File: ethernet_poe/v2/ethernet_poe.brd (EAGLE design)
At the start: 45.5 x 50.5 mm, 86 parts, among them J3 ARJM11C7-104-AB-EW2, Q1 BSR16, U1 AZ1117EH-3.3TRG1, U2 IFX91041, U3 W5500, U4 TPS26600PWPR, X1 25MHz

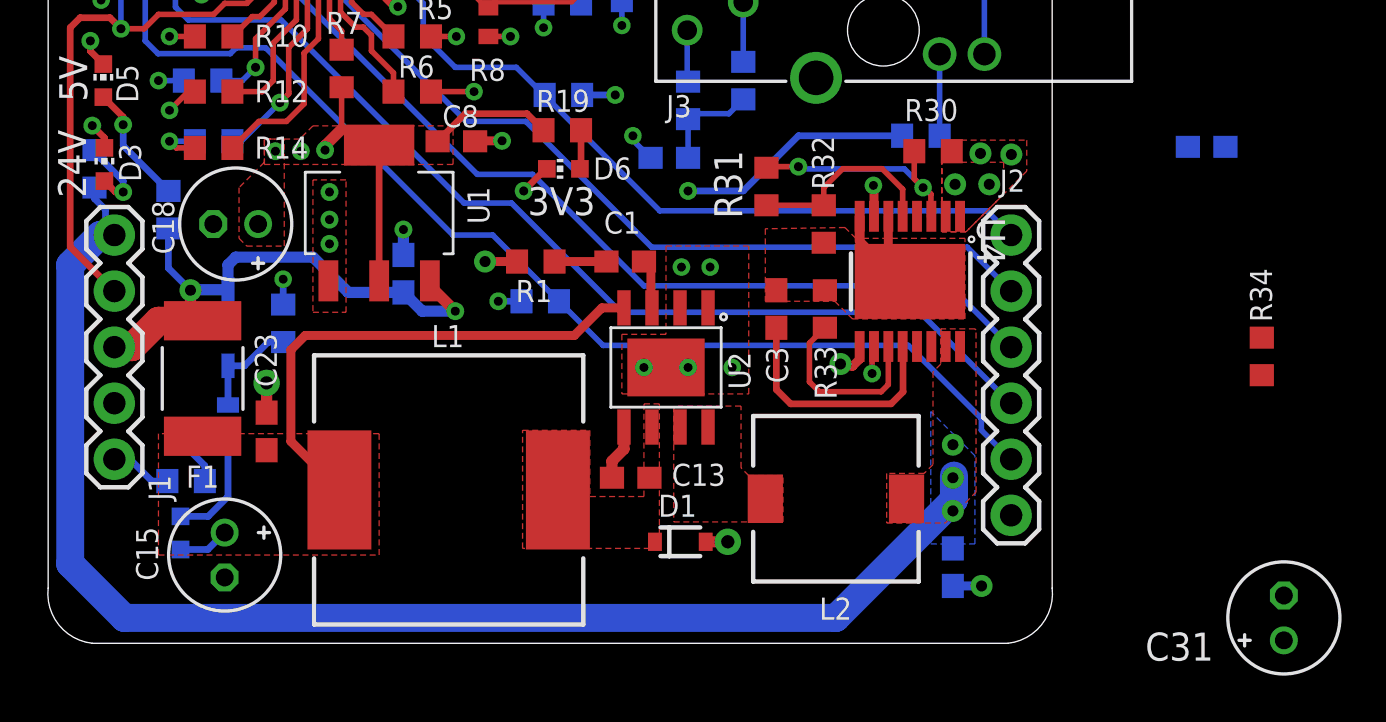
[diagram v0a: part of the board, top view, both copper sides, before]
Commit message: Placed + routed bulk 24v capacitor
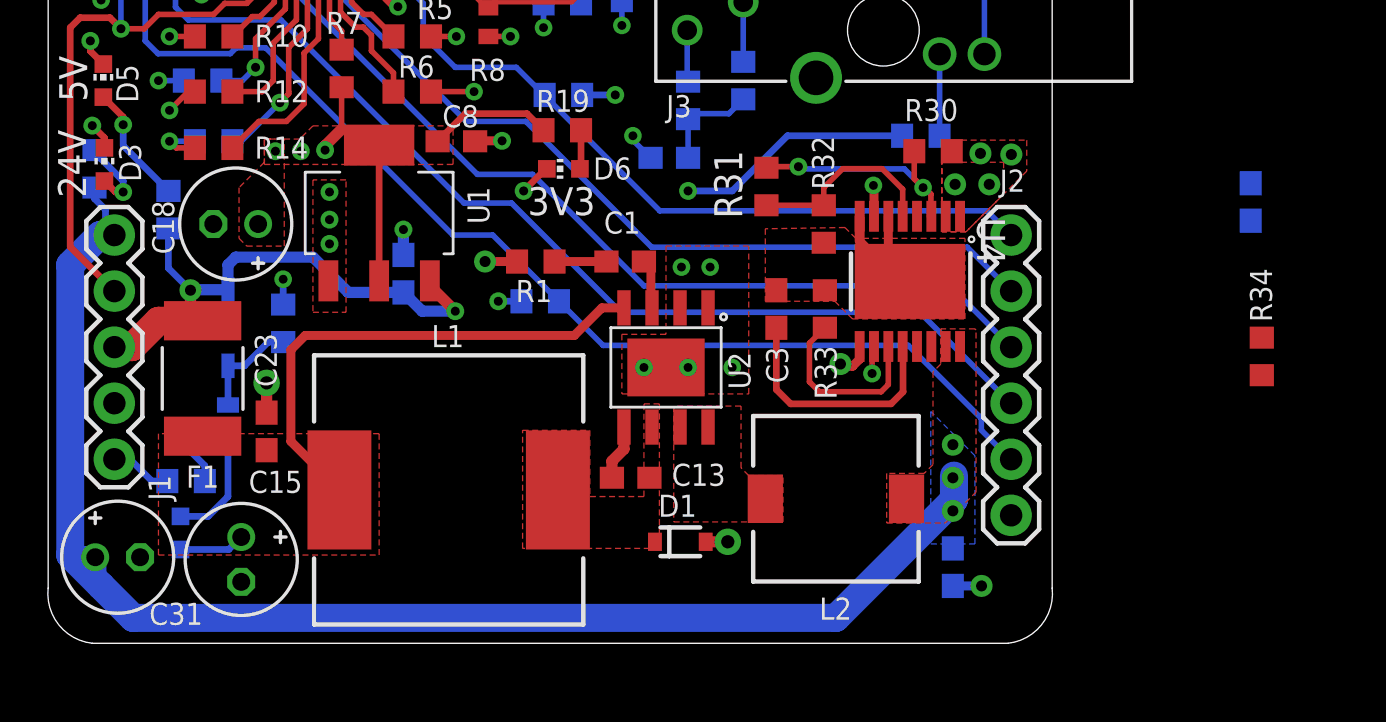
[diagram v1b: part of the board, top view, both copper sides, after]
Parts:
- moved C31 52.9 mm to (2.15, 3.40), turned to 0 degrees
- moved C30 3.20 mm to (53.5, 19.5), turned to 270 degrees
- moved C15 0.78 mm to (7.75, 3.30)
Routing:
- net +24V_FUSE: track 63.2 -> 65.6 mm
- net +5V_PREFUSE: track 25.5 -> 26.1 mm
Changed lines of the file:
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@@
 <attribute name="VALUE" x="13.195" y="15.615" size="1.27" layer="28" rot="MR90"/>
 </element>
-<element name="C15" library="rcl" library_urn="urn:adsk.eagle:library:334" package="E2-5" package3d_urn="urn:adsk.eagle:package:23346/2" value="100uF" x="7" y="3.5" smashed="yes" rot="R270">
-<attribute name="NAME" x="3.984" y="2.34" size="1" layer="25" font="vector" rot="R90"/>
-<attribute name="POPULARITY" value="7" x="7" y="3.5" size="1.778" layer="27" rot="R270" display="off"/>
-<attribute name="SPICEPREFIX" value="C" x="7" y="3.5" size="1.778" layer="27" rot="R270" display="off"/>
-<attribute name="VALUE" x="4.841" y="0.96" size="1.27" layer="27" ratio="10" rot="R270"/>
+<element name="C15" library="rcl" library_urn="urn:adsk.eagle:library:334" package="E2-5" package3d_urn="urn:adsk.eagle:package:23346/2" value="100uF" x="7.75" y="3.3" smashed="yes" rot="R270">
+<attribute name="NAME" x="8.09" y="6.316" size="1" layer="25" font="vector"/>
+<attribute name="POPULARITY" value="7" x="7.75" y="3.3" size="1.778" layer="27" rot="R270" display="off"/>
+<attribute name="SPICEPREFIX" value="C" x="7.75" y="3.3" size="1.778" layer="27" rot="R270" display="off"/>
+<attribute name="VALUE" x="5.591" y="0.76" size="1.27" layer="27" ratio="10" rot="R270"/>
 </element>
 <element name="J1" library="SparkFun-Connectors" package="1X05" package3d_urn="urn:adsk.eagle:package:38104/1" value="" x="2" y="18" smashed="yes" rot="R270">
@@
 <attribute name="VALUE" x="33.905" y="14.015" size="1.27" layer="27" rot="R90"/>
 </element>
-<element name="C30" library="rcl" library_urn="urn:adsk.eagle:library:334" package="C0603" package3d_urn="urn:adsk.eagle:package:23616/2" value="1uF" x="51.5" y="22" smashed="yes" rot="MR180">
-<attribute name="NAME" x="50.865" y="21.365" size="1.27" layer="26" rot="MR180"/>
-<attribute name="POPULARITY" value="37" x="51.5" y="22" size="1.778" layer="28" rot="MR180" display="off"/>
-<attribute name="SPICEPREFIX" value="C" x="51.5" y="22" size="1.778" layer="28" rot="MR180" display="off"/>
-<attribute name="VALUE" x="50.865" y="23.905" size="1.27" layer="28" rot="MR180"/>
+<element name="C30" library="rcl" library_urn="urn:adsk.eagle:library:334" package="C0603" package3d_urn="urn:adsk.eagle:package:23616/2" value="1uF" x="53.5" y="19.5" smashed="yes" rot="MR270">
+<attribute name="NAME" x="52.865" y="20.135" size="1.27" layer="26" rot="MR270"/>
+<attribute name="POPULARITY" value="37" x="53.5" y="19.5" size="1.778" layer="28" rot="MR270" display="off"/>
+<attribute name="SPICEPREFIX" value="C" x="53.5" y="19.5" size="1.778" layer="28" rot="MR270" display="off"/>
+<attribute name="VALUE" x="55.405" y="20.135" size="1.27" layer="28" rot="MR270"/>
 </element>
 <element name="R33" library="rcl" library_urn="urn:adsk.eagle:library:334" package="R0603" package3d_urn="urn:adsk.eagle:package:23555/3" value="11.8k 1%" x="34.2" y="14.65" smashed="yes" rot="R90">
@@
 <attribute name="VALUE" x="52.095" y="13.135" size="1.27" layer="27" rot="R270"/>
 </element>
-<element name="C31" library="rcl" library_urn="urn:adsk.eagle:library:334" package="E2-5" package3d_urn="urn:adsk.eagle:package:23346/2" value="2.2mF" x="55" y="0.65" smashed="yes" rot="R90">
-<attribute name="NAME" x="51.81" y="-0.016" size="1.27" layer="25" ratio="10" rot="R180"/>
-<attribute name="POPULARITY" value="7" x="55" y="0.65" size="1.778" layer="27" rot="R90" display="off"/>
-<attribute name="SPICEPREFIX" value="C" x="55" y="0.65" size="1.778" layer="27" rot="R90" display="off"/>
-<attribute name="VALUE" x="57.159" y="3.19" size="1.27" layer="27" ratio="10" rot="R90"/>
+<element name="C31" library="rcl" library_urn="urn:adsk.eagle:library:334" package="E2-5" package3d_urn="urn:adsk.eagle:package:23346/2" value="2.2mF" x="2.15" y="3.4" smashed="yes">
+<attribute name="NAME" x="6.01" y="1.334" size="1" layer="25" rot="R180"/>
+<attribute name="POPULARITY" value="7" x="2.15" y="3.4" size="1.778" layer="27" display="off"/>
+<attribute name="SPICEPREFIX" value="C" x="2.15" y="3.4" size="1.778" layer="27" display="off"/>
+<attribute name="VALUE" x="4.69" y="1.241" size="1.27" layer="27" ratio="10"/>
 </element>
 </elements>
@@
 <wire x1="20.85" y1="44.2" x2="20.5" y2="44.55" width="0.4064" layer="16"/>
 <via x="20.5" y="44.55" extent="1-16" drill="0.4064"/>
-<wire x1="35.774996875" y1="12.949996875" x2="52.35" y2="22" width="0" layer="19" extent="1-16"/>
-<wire x1="55" y1="1.666" x2="42.64" y2="5.3" width="0" layer="19" extent="1-1"/>
+<wire x1="35.774996875" y1="12.949996875" x2="53.5" y2="18.65" width="0" layer="19" extent="1-16"/>
+<wire x1="3.166" y1="3.4" x2="42.64" y2="5.3" width="0" layer="19" extent="1-1"/>
 </signal>
 <signal name="N$13">
@@
 <vertex x="19" y="25.75"/>
 <vertex x="19" y="21.5"/>
-<vertex x="20" y="20.5"/>
-<vertex x="26" y="20.5"/>
+<vertex x="26" y="21.5"/>
 <vertex x="26" y="25.75"/>
 </polygon>
@@
 <contactref element="C27" pad="1"/>
 <via x="28" y="20" extent="1-16" drill="0.4064"/>
-<wire x1="33.00289375" y1="22.5" x2="30.50289375" y2="20" width="0.3048" layer="16"/>
-<wire x1="30.50289375" y1="20" x2="28" y2="20" width="0.3048" layer="16"/>
-<wire x1="37.7" y1="22.5" x2="33.00289375" y2="22.5" width="0.3048" layer="16"/>
+<wire x1="32.50289375" y1="22.5" x2="30.00289375" y2="20" width="0.3048" layer="16"/>
+<wire x1="30.00289375" y1="20" x2="28" y2="20" width="0.3048" layer="16"/>
+<wire x1="37.7" y1="22.5" x2="32.50289375" y2="22.5" width="0.3048" layer="16"/>
 <wire x1="17.55" y1="43.5" x2="19.15" y2="43.5" width="0.4064" layer="16"/>
 <wire x1="17.5" y1="42.3" x2="17.5" y2="43.45" width="0.4064" layer="1"/>
@@
 <wire x1="36.425" y1="20.225" x2="36.4" y2="20.25" width="0.3048" layer="1"/>
 <via x="36.4" y="20.25" extent="1-16" drill="0.4"/>
-<wire x1="42.65" y1="21.65" x2="50.65" y2="22" width="0" layer="19" extent="16-16"/>
+<wire x1="42.65" y1="21.65" x2="53.5" y2="20.35" width="0" layer="19" extent="16-16"/>
 </signal>
 <signal name="N$14">
@@
 <wire x1="10" y1="8.65" x2="10" y2="12.8" width="0.4064" layer="1"/>
 <wire x1="10" y1="12.8" x2="10.65" y2="13.45" width="0.4064" layer="1"/>
-<wire x1="7" y1="4.516" x2="6.234" y2="3.75" width="0.3048" layer="16"/>
-<wire x1="6.234" y1="3.75" x2="5" y2="3.75" width="0.3048" layer="16"/>
+<wire x1="7.75" y1="4.316" x2="7.184" y2="3.75" width="0.3048" layer="16"/>
+<wire x1="7.184" y1="3.75" x2="5" y2="3.75" width="0.3048" layer="16"/>
 </signal>
 <signal name="N$23">
@@
 <wire x1="40.05" y1="7.1" x2="40.05" y2="6" width="1.27" layer="16"/>
 <wire x1="40.05" y1="6" x2="34.7" y2="0.65" width="1.27" layer="16"/>
-<wire x1="34.7" y1="0.65" x2="2.45" y2="0.65" width="1.27" layer="16"/>
-<wire x1="2.45" y1="0.65" x2="0" y2="3.1" width="1.27" layer="16"/>
-<wire x1="0" y1="3.1" x2="0" y2="16.65" width="1.27" layer="16"/>
+<wire x1="34.7" y1="0.65" x2="2.85" y2="0.65" width="1.27" layer="16"/>
+<wire x1="2.85" y1="0.65" x2="1.4" y2="2.1" width="1.27" layer="16"/>
+<wire x1="1.4" y1="2.1" x2="0" y2="3.5" width="1.27" layer="16"/>
 <contactref element="U4" pad="15"/>
 <contactref element="U4" pad="16"/>
@@
 <via x="40" y="8.5" extent="1-16" drill="0.5"/>
 <contactref element="R17" pad="1"/>
+<wire x1="0" y1="3.5" x2="0" y2="16.65" width="1.27" layer="16"/>
 <wire x1="2" y1="18" x2="1.6" y2="18" width="0.3048" layer="16"/>
 <wire x1="1.6" y1="19.15" x2="1.6" y2="18" width="0.3048" layer="16"/>
 <wire x1="1.6" y1="19.15" x2="1.1" y2="19.65" width="0.3048" layer="16"/>
 <wire x1="1.1" y1="19.65" x2="1.1" y2="20.15" width="0.3048" layer="16"/>
-<wire x1="40" y1="3.8" x2="55" y2="-0.366" width="0" layer="19" extent="16-16"/>
+<wire x1="1.134" y1="3.4" x2="1.134" y2="2.366" width="1.016" layer="16"/>
+<wire x1="1.134" y1="2.366" x2="1.4" y2="2.1" width="1.016" layer="16"/>
+<wire x1="1.134" y1="3.4" x2="0.1" y2="3.4" width="1.016" layer="16"/>
+<wire x1="0.1" y1="3.4" x2="0" y2="3.5" width="1.016" layer="16"/>
 </signal>
 <signal name="N$9">
@@
 <wire x1="36.3384" y1="12.863396875" x2="36.3384" y2="11.7263" width="0.254" layer="1"/>
 <via x="36.3384" y="11.7263" extent="1-16" drill="0.4064"/>
-<wire x1="36.3384" y1="11.7263" x2="36.3384" y2="11.71431875" width="0.254" layer="16"/>
+<wire x1="36.3384" y1="11.71431875" x2="36.3384" y2="11.7263" width="0.254" layer="16"/>
 <wire x1="36.425" y1="12.949996875" x2="54" y2="13.35" width="0" layer="19" extent="1-1"/>
 </signal>

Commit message: Pre Review Commit, Completed Routing
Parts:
- added H1, H2: MOUNT-PAD-ROUND2.8, holes:2,8-PAD
- J2: device SparkFun-Connectors:1X06 -> SparkFun-Connectors:1X07
- moved C30 21.5 mm to (32.0, 19.5), flipped to the top
- moved R34 20.0 mm to (34.1, 10.6), flipped to the bottom, turned to 0 degrees
- moved R31 3.94 mm to (35.0, 22.1), turned to 180 degrees
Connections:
- net 24_LOAD: now also J2.7
- net GND: now also H1.B2,8, H2.B2,8
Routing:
- net 24_LOAD: track 1.27 -> 21.5 mm
- net N$32: track 6.54 -> 12.8 mm, vias 0 -> 2
- net N$9: track 10.9 -> 5.83 mm, vias 2 -> 1
- net +3V3_D: track 38.9 -> 36.3 mm
- net +24V_FUSE: track 65.6 -> 63.5 mm
- net +24V: track 1.41 -> 2.56 mm, vias 5 -> 6
- net MOSI: track 44.7 -> 45.5 mm
- net N$33: track 8.36 -> 7.59 mm
- net !INTN: track 41.6 -> 42.4 mm
- net GND: track 57.1 -> 57.4 mm, vias 57 -> 58

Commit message: Additional design review updates
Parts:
- added U$2: (no value), RoboJackets-Aesthetics:ROBOBUZZ_0.4X
- C1: value 22nF -> 22nF, 50V
- C27, C28: value (none) -> TBD
- C3: value 2.2uF -> 2.2uF, 50V
- C30: value 1uF -> 1uF, 50V
- C31: value 2.2mF -> 2.2mF, 50V
- moved D4 7.65 mm to (12.5, 6.00)
- moved C16 1.12 mm to (16.1, 16.8)
- moved C1 1.12 mm to (26.1, 17.3)
- moved C10 1.12 mm to (12.1, 41.5)
- moved C11 1.12 mm to (10.8, 35.4)
- moved C12 1.12 mm to (13.7, 34.3)
- moved C13 1.12 mm to (26.4, 7.50)
- moved C14 1.12 mm to (13.7, 33.0)
- moved C15 1.12 mm to (8.75, 3.80)
- moved C17 1.12 mm to (17.4, 45.9)
- moved C18 1.12 mm to (8.50, 19.0)
- moved C19 1.12 mm to (41.0, 3.45)
- moved C2 1.12 mm to (3.50, 38.0)
- moved C20 1.12 mm to (6.15, 36.6)
- moved C21 1.12 mm to (26.0, 30.0)
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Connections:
- new net !RST: C17.1, R20.1, S1.2.1, S1.2.2
- net !RSTN: no longer C17.1, R20.1, S1.2.1, S1.2.2
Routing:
- net !RSTN: track 55.5 -> 45.4 mm
- net !RST: track 0.00 -> 7.00 mm
- net +5V_PREFUSE: track 26.1 -> 27.1 mm
- net N$23: track 4.77 -> 5.62 mm
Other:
- outline, holes or cut-outs redrawn
- board text added: "5V BAD"
- board text added: "PoE v2.0"
- board text added: "RoboJackets RoboRacing July 2020"
- board text removed: "RoboRacing POE v1.2 2020"

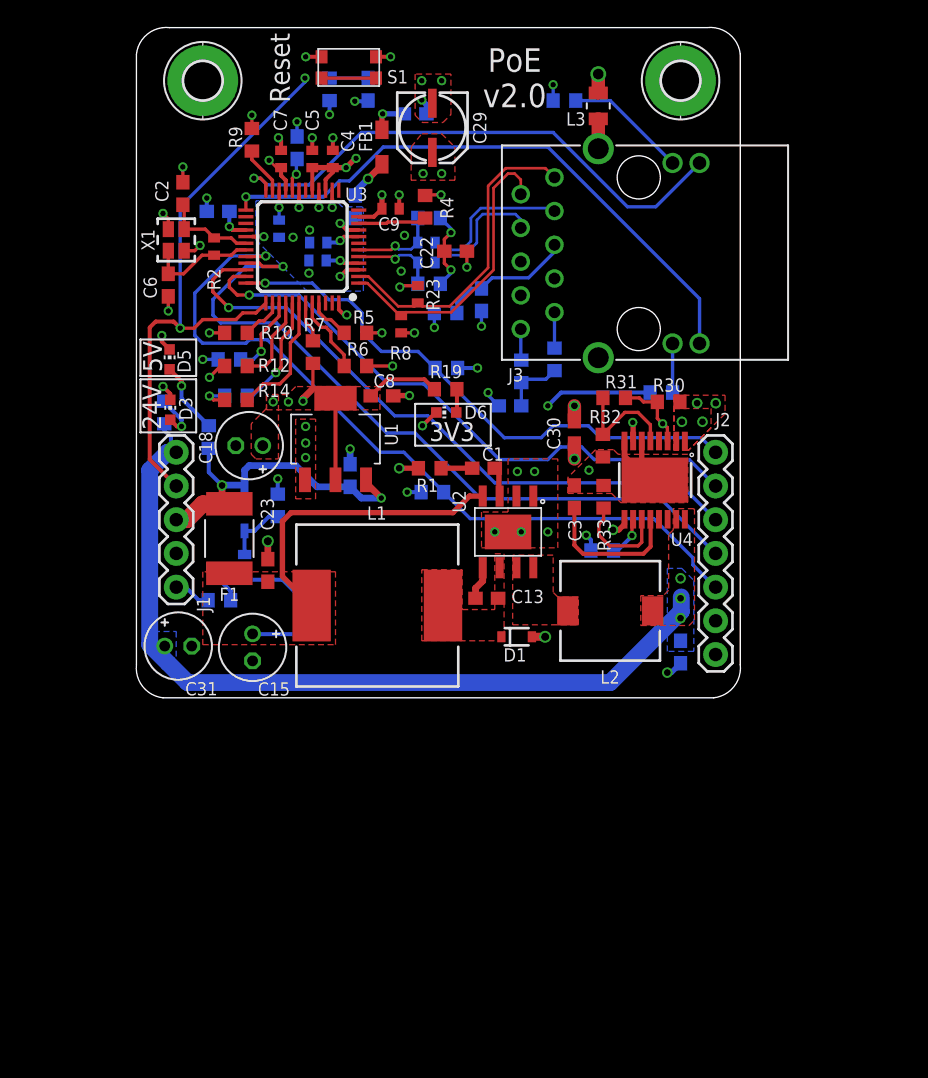
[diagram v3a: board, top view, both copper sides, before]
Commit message: Made drc compliant
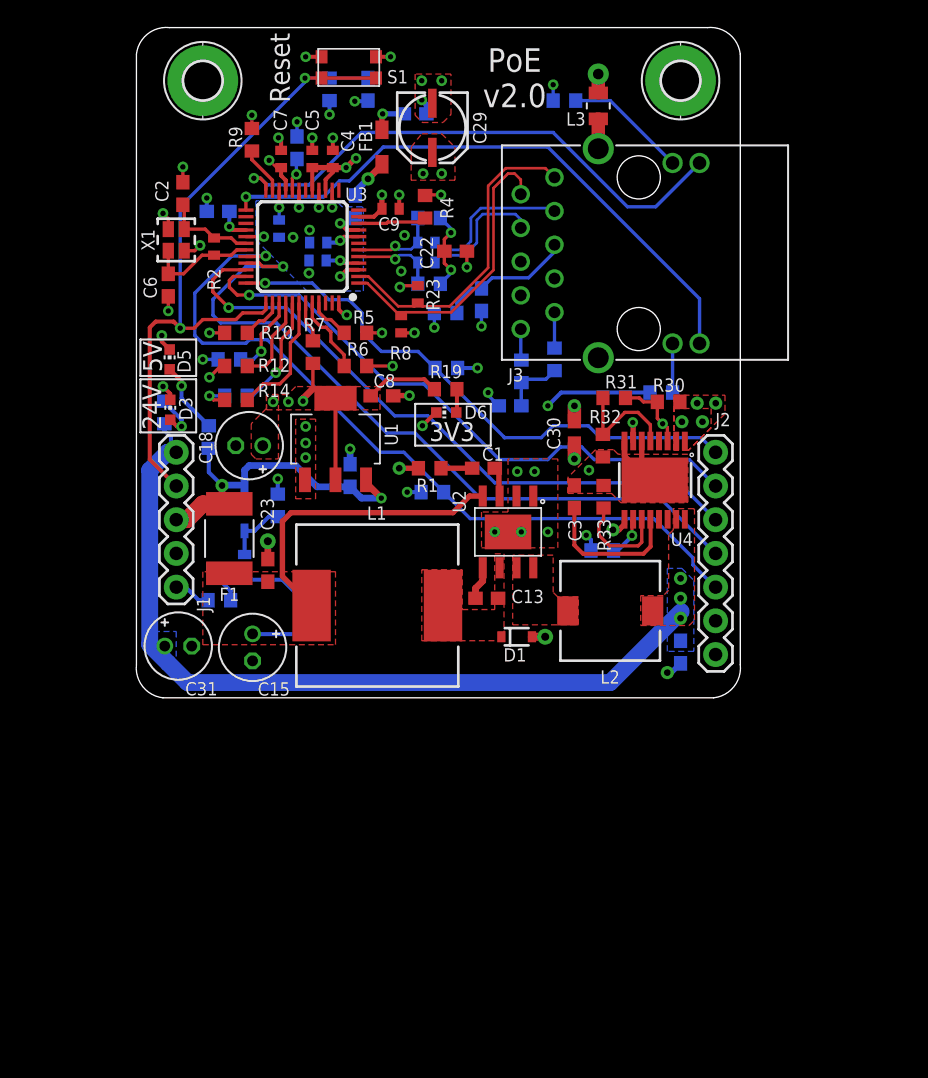
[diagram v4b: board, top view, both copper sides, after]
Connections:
- net !INTN renamed !INT
- removed net !RSTN: J1.2, U3.37
- net !RST: now also J1.2, U3.37
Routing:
- net !RST: track 7.00 -> 55.8 mm, vias 0 -> 2
- net !RSTN: track 45.4 -> 0.00 mm, vias 2 -> 0
- net +24V_FUSE: track 63.5 -> 62.4 mm

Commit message: DRC fixes
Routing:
- net GND: track 57.1 -> 57.7 mm

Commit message: Began design review changes
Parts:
- added D7: YLW, led:CHIP-LED0603
- added D8: BLU, led:CHIP-LED0603
- added D9: 1N4148W-7-F, ethernet_poe:SOD123_DIO
- added R35, R36: 470, rcl:R0603
- C16: value 1 uF -> 1uF
- C19: value 10nF, 50V -> 10000pF, 50V
- C22, C24, C25, C26: value 10nF -> 10000pF
- R18: value 600 -> 330
- R19: value 220 -> 470
- R23, R8: value 49 -> 49, 1%
- R24: value 22 -> 22, 1%
- R29, R3: value 75 -> 75, 1%
- R30: value 715k -> 715k, 1%
- R31: value 20k -> 20k, 1%
- R32: value 30.1k -> 30.1k, 1%
- R33: value 11.8k 1% -> 11.8k, 1%
- R34: value 33.2k -> 66.5k, 1%
- R4: value 12.4k 1% -> 12.4k, 1%
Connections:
- net !SCSN renamed !SCS
- net N$14 renamed 5V_RAW
- net N$29 renamed CT
- net N$30 renamed Y_LED+
- net N$31 renamed G_LED+
- net N$32 renamed RTN
- new net 3V3_LED1: D7.A, R35.2
- new net 3V3_LED2: D8.A, R36.2
- new net ACTLED: D7.C, U3.27
- new net DUPLED: D8.C, U3.26
- net +3V3_D: now also D9.2, R35.1, R36.1
- net +5V: now also D9.1
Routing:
- net RX_FILTER: track 6.03 -> 7.24 mm
- net GND: track 57.7 -> 57.9 mm, vias 58 -> 62
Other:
- board text added: "#3"
